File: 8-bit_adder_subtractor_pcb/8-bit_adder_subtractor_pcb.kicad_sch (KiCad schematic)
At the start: 6 parts, among them U1 74LS86, U2 74LS86, U3 74LS08, U4 74LS08, U5 74LS32, U6 74LS86

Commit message: Redesigned DDPT switch footprint
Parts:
- added D1, D2, D3, D4, D5, D6, D7, D8: ValueA, LED_THT:LED_D3.0mm, symbol Device:LED
- added D10, D11, D12, D13, D14, D15, D16, D9: ValueB, LED_THT:LED_D3.0mm, symbol Device:LED
- added D17, D18, D19, D20, D21, D22, D23, D24: Total, LED_THT:LED_D3.0mm, symbol Device:LED
- added D25: Subtraction, LED_THT:LED_D3.0mm, symbol Device:LED
- added D26: Addition, LED_THT:LED_D3.0mm, symbol Device:LED
- added R1, R10, R11, R12, R13, R14, R15, R16, R17, R18, R19, R2, R20, R21, R22, R23, R24, R25, R27, R3, R4, R5, R6, R7, R8, R9: 220, Resistor_THT:R_Axial_DIN0207_L6.3mm_D2.5mm_P7.62mm_Horizontal, symbol Device:R
- added R26: 10K, Resistor_THT:R_Axial_DIN0207_L6.3mm_D2.5mm_P7.62mm_Horizontal, symbol Device:R
- added SW1, SW10, SW11, SW12, SW13, SW14, SW15, SW16, SW17, SW2, SW3, SW4, SW5, SW6, SW7, SW8, SW9: SW_DPDT_x2, ddpt:SWITCH_S20203, symbol Switch:SW_DPDT_x2
- added U10, U7, U8: 74LS86, Package_DIP:DIP-14_W7.62mm, symbol 74xx:74LS86
- added U11, U9: 74LS08, Package_DIP:DIP-14_W7.62mm, symbol 74xx:74LS08
- added U12: 74LS32, Package_DIP:DIP-14_W7.62mm, symbol 74xx:74LS32
- U1, U2, U3, U4, U5, U6: footprint (none) -> Package_DIP:DIP-14_W7.62mm
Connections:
- net Cout0 is gone; now on net Cin1: U5.3
- net Cout1 is gone; now on net Cin2: U5.6
- net Cout2 is gone; now on net Cin3: U5.8
- net SL is gone; now on net Cin0: U6.1, U6.12, U6.4, U6.9
- net A0: now also R1.1, SW1.3 (C), SW1.6 (C)
- net A1: now also R2.1, SW2.3 (C), SW2.6 (C)
- net A2: now also R3.1, SW3.3 (C), SW3.6 (C)
- net A3: now also R4.1, SW4.3 (C), SW4.6 (C)
- net B0: now also R9.1, SW9.3 (C), SW9.6 (C)
- net B1: now also R10.1, SW10.3 (C), SW10.6 (C)
- net B2: now also R11.1, SW11.3 (C), SW11.6 (C)
- net B3: now also R12.1, SW12.3 (C), SW12.6 (C)
- net Cin0: now also R25.1, R26.1, SW17.3 (C), SW17.6 (C), U7.1, U7.12, U7.4, U7.9
- net VCC: now reaches U5.14 (VCC)
- net VCC: now also U1.14 (VCC), U2.14 (VCC), U3.14 (VCC), U4.14 (VCC), U6.14 (VCC), SW1.2 (B), SW1.5 (B), SW10.2 (B), SW10.5 (B), SW11.2 (B), SW11.5 (B), SW12.2 (B), SW12.5 (B), SW13.2 (B), SW13.5 (B), SW14.2 (B), SW14.5 (B), SW15.2 (B), SW15.5 (B), SW16.2 (B), SW16.5 (B), SW17.2 (B), SW17.5 (B), SW2.2 (B), SW2.5 (B), SW3.2 (B), SW3.5 (B), SW4.2 (B), SW4.5 (B), SW5.2 (B), SW5.5 (B), SW6.2 (B), SW6.5 (B), SW7.2 (B), SW7.5 (B), SW8.2 (B), SW8.5 (B), SW9.2 (B), SW9.5 (B), U10.14 (VCC), U11.14 (VCC), U12.14 (VCC), U7.14 (VCC), U8.14 (VCC), U9.14 (VCC)
- net GND: now reaches U5.7 (GND)
- net GND: now also U1.7 (GND), U2.7 (GND), U3.7 (GND), U4.7 (GND), U6.7 (GND), D1.1 (K), D10.1 (K), D11.1 (K), D12.1 (K), D13.1 (K), D14.1 (K), D15.1 (K), D16.1 (K), D17.1 (K), D18.1 (K), D19.1 (K), D2.1 (K), D20.1 (K), D21.1 (K), D22.1 (K), D23.1 (K), D24.1 (K), D25.1 (K), D26.1 (K), D3.1 (K), D4.1 (K), D5.1 (K), D6.1 (K), D7.1 (K), D8.1 (K), D9.1 (K), R26.2, U10.7 (GND), U11.7 (GND), U12.7 (GND), U7.7 (GND), U8.7 (GND), U9.7 (GND)
- net S3: now reaches U2.11
- net S3: now also R20.1
- net S0: now reaches U2.3
- net S0: now also R17.1
- net S2: now reaches U2.8
- net S2: now also R19.1
- net S1: now reaches U2.6
- net S1: now also R18.1
- net Cout3 renamed Cin4
- net Cin4: now also U10.2, U11.1
- new net: D17.2 (A), R17.2
- new net: SW3.1 (A), SW3.4 (A)
- new net: SW11.1 (A), SW11.4 (A)
- new net: SW4.1 (A), SW4.4 (A)
- new net: SW13.1 (A), SW13.4 (A)
- new net: SW15.1 (A), SW15.4 (A)
- new net: D2.2 (A), R2.2
- new net: D15.2 (A), R15.2
- new net: SW6.1 (A), SW6.4 (A)
- new net: D11.2 (A), R11.2
- new net: SW2.1 (A), SW2.4 (A)
- new net: U10.1, U11.2, U8.3
- new net: U11.3, U12.2
- new net: D22.2 (A), R22.2
- new net: D24.2 (A), R24.2
- new net: SW10.1 (A), SW10.4 (A)
- new net: U10.12, U11.13, U8.11
- new net: U7.11, U8.13, U9.13
- new net: D21.2 (A), R21.2
- new net: D14.2 (A), R14.2
- new net: U11.11, U12.13
- new net: D8.2 (A), R8.2
- new net: D1.2 (A), R1.2
- new net: U7.8, U8.10, U9.10
- new net: U10.9, U11.10, U8.8
- new net: SW7.1 (A), SW7.4 (A)
- new net: U12.4, U9.6
- new net: U11.6, U12.5
- new net: SW5.1 (A), SW5.4 (A)
- new net: D19.2 (A), R19.2
- new net: D16.2 (A), R16.2
- new net: D12.2 (A), R12.2
- new net: D7.2 (A), R7.2
- new net: U7.6, U8.5, U9.5
- new net: SW9.1 (A), SW9.4 (A)
- new net: U7.3, U8.2, U9.2
- new net: U12.1, U9.3
- new net: R27.1, SW17.1 (A), SW17.4 (A)
- new net: U12.9, U9.8
- new net: D26.2 (A), R27.2
- new net: U10.4, U11.5, U8.6
- new net: D9.2 (A), R9.2
- new net: D25.2 (A), R25.2
- new net: D6.2 (A), R6.2
- new net: SW16.1 (A), SW16.4 (A)
- new net: SW1.1 (A), SW1.4 (A)
- new net: D18.2 (A), R18.2
- new net: D3.2 (A), R3.2
- new net: D20.2 (A), R20.2
- new net: D23.2 (A), R23.2
- new net: SW8.1 (A), SW8.4 (A)
- new net: D10.2 (A), R10.2
- new net: D5.2 (A), R5.2
- new net: D4.2 (A), R4.2
- new net: U11.8, U12.10
- new net: D13.2 (A), R13.2
- new net: SW14.1 (A), SW14.4 (A)
- new net: U12.12, U9.11
- new net: SW12.1 (A), SW12.4 (A)
- new net A4: R5.1, SW5.3 (C), SW5.6 (C), U8.1, U9.1
- new net A5: R6.1, SW6.3 (C), SW6.6 (C), U8.4, U9.4
- new net A6: R7.1, SW7.3 (C), SW7.6 (C), U8.9, U9.9
- new net A7: R8.1, SW8.3 (C), SW8.6 (C), U8.12, U9.12
- new net B4: R13.1, SW13.3 (C), SW13.6 (C), U7.2
- new net B5: R14.1, SW14.3 (C), SW14.6 (C), U7.5
- new net B6: R15.1, SW15.3 (C), SW15.6 (C), U7.10
- new net B7: R16.1, SW16.3 (C), SW16.6 (C), U7.13
- new net Cin5: U10.5, U11.4, U12.3
- new net Cin6: U10.10, U11.9, U12.6
- new net Cin7: U10.13, U11.12, U12.8
- new net Cout7: U12.11
- new net S4: R21.1, U10.3
- new net S5: R22.1, U10.6
- new net S6: R23.1, U10.8
- new net S7: R24.1, U10.11
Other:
- note added: "When the switch is turned on then the select and Cin0 is tied to Vcc and the circuit acts as subtractor."
- moved on the sheet: U1E, U2A, U2B, U2C, U2D, U2E, U3E, U4A, U4B, U4C, U4D, U4E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

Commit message: added the pcb files
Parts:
- added D27: Carry, LED_THT:LED_D3.0mm, symbol Device:LED
- added J1: Barrel_Jack, Connector_BarrelJack:BarrelJack_Horizontal, symbol Connector:Barrel_Jack
- added R28: 220, Resistor_THT:R_Axial_DIN0207_L6.3mm_D2.5mm_P7.62mm_Horizontal, symbol Device:R
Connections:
- net A0: now also SW1.2 (B), SW1.5 (B); no longer SW1.3 (C), SW1.6 (C)
- net A1: now also SW2.2 (B), SW2.5 (B); no longer SW2.3 (C), SW2.6 (C)
- net A2: now also SW3.2 (B), SW3.5 (B); no longer SW3.3 (C), SW3.6 (C)
- net A3: now also SW4.2 (B), SW4.5 (B); no longer SW4.3 (C), SW4.6 (C)
- net A4: now also SW5.2 (B), SW5.5 (B); no longer SW5.3 (C), SW5.6 (C)
- net A5: now also SW6.2 (B), SW6.5 (B); no longer SW6.3 (C), SW6.6 (C)
- net A6: now also SW7.2 (B), SW7.5 (B); no longer SW7.3 (C), SW7.6 (C)
- net A7: now also SW8.2 (B), SW8.5 (B); no longer SW8.3 (C), SW8.6 (C)
- net B0: now also SW9.2 (B), SW9.5 (B); no longer SW9.3 (C), SW9.6 (C)
- net B1: now also SW10.2 (B), SW10.5 (B); no longer SW10.3 (C), SW10.6 (C)
- net B2: now also SW11.2 (B), SW11.5 (B); no longer SW11.3 (C), SW11.6 (C)
- net B3: now also SW12.2 (B), SW12.5 (B); no longer SW12.3 (C), SW12.6 (C)
- net B4: now also SW13.2 (B), SW13.5 (B); no longer SW13.3 (C), SW13.6 (C)
- net B5: now also SW14.2 (B), SW14.5 (B); no longer SW14.3 (C), SW14.6 (C)
- net B6: now also SW15.2 (B), SW15.5 (B); no longer SW15.3 (C), SW15.6 (C)
- net B7: now also SW16.2 (B), SW16.5 (B); no longer SW16.3 (C), SW16.6 (C)
- net Cout7: now also R28.1
- net GND: now also SW1.1 (A), SW1.4 (A), SW10.1 (A), SW10.4 (A), SW11.1 (A), SW11.4 (A), SW12.1 (A), SW12.4 (A), SW13.1 (A), SW13.4 (A), SW14.1 (A), SW14.4 (A), SW15.1 (A), SW15.4 (A), SW16.1 (A), SW16.4 (A), SW2.1 (A), SW2.4 (A), SW3.1 (A), SW3.4 (A), SW4.1 (A), SW4.4 (A), SW5.1 (A), SW5.4 (A), SW6.1 (A), SW6.4 (A), SW7.1 (A), SW7.4 (A), SW8.1 (A), SW8.4 (A), SW9.1 (A), SW9.4 (A), D27.1 (K), J1.2
- net VCC: now also SW1.3 (C), SW1.6 (C), SW10.3 (C), SW10.6 (C), SW11.3 (C), SW11.6 (C), SW12.3 (C), SW12.6 (C), SW13.3 (C), SW13.6 (C), SW14.3 (C), SW14.6 (C), SW15.3 (C), SW15.6 (C), SW16.3 (C), SW16.6 (C), SW2.3 (C), SW2.6 (C), SW3.3 (C), SW3.6 (C), SW4.3 (C), SW4.6 (C), SW5.3 (C), SW5.6 (C), SW6.3 (C), SW6.6 (C), SW7.3 (C), SW7.6 (C), SW8.3 (C), SW8.6 (C), SW9.3 (C), SW9.6 (C), J1.1; no longer SW1.2 (B), SW1.5 (B), SW10.2 (B), SW10.5 (B), SW11.2 (B), SW11.5 (B), SW12.2 (B), SW12.5 (B), SW13.2 (B), SW13.5 (B), SW14.2 (B), SW14.5 (B), SW15.2 (B), SW15.5 (B), SW16.2 (B), SW16.5 (B), SW2.2 (B), SW2.5 (B), SW3.2 (B), SW3.5 (B), SW4.2 (B), SW4.5 (B), SW5.2 (B), SW5.5 (B), SW6.2 (B), SW6.5 (B), SW7.2 (B), SW7.5 (B), SW8.2 (B), SW8.5 (B), SW9.2 (B), SW9.5 (B)
- net Cin0 renamed SL
- new net: D27.2 (A), R28.2
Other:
- moved on the sheet: SW10A, SW10B, SW11A, SW11B, SW12A, SW12B, SW13A, SW13B, SW14A, SW14B, SW15A, SW15B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

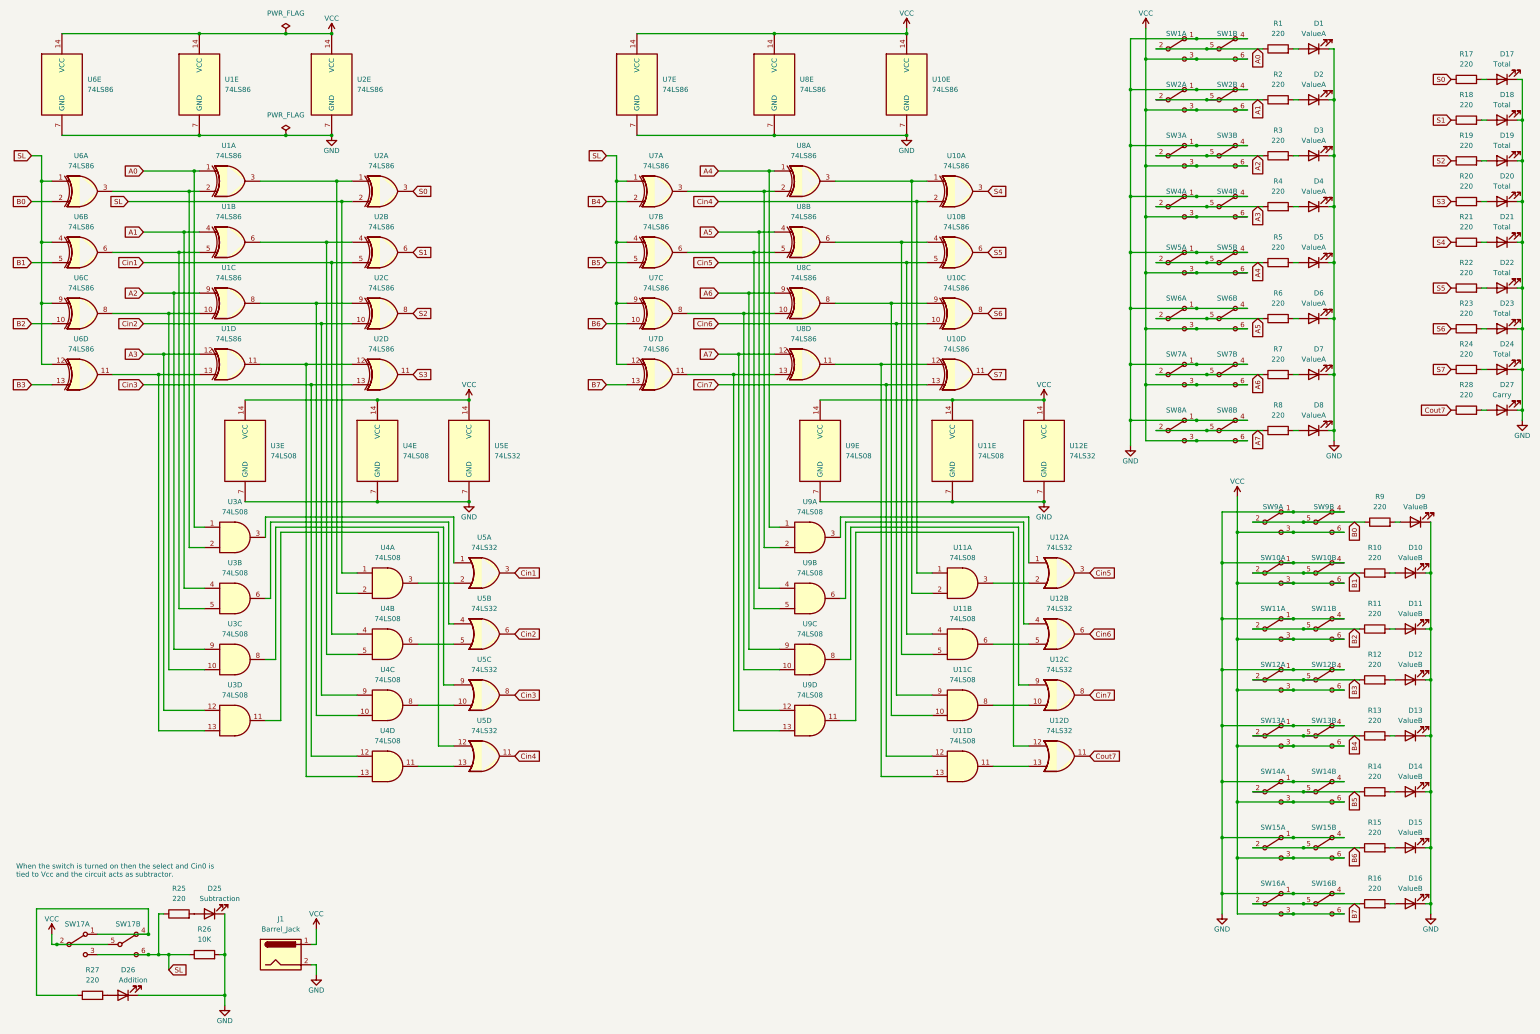
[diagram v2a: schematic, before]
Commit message: Edited the Silkscreen for LAB448
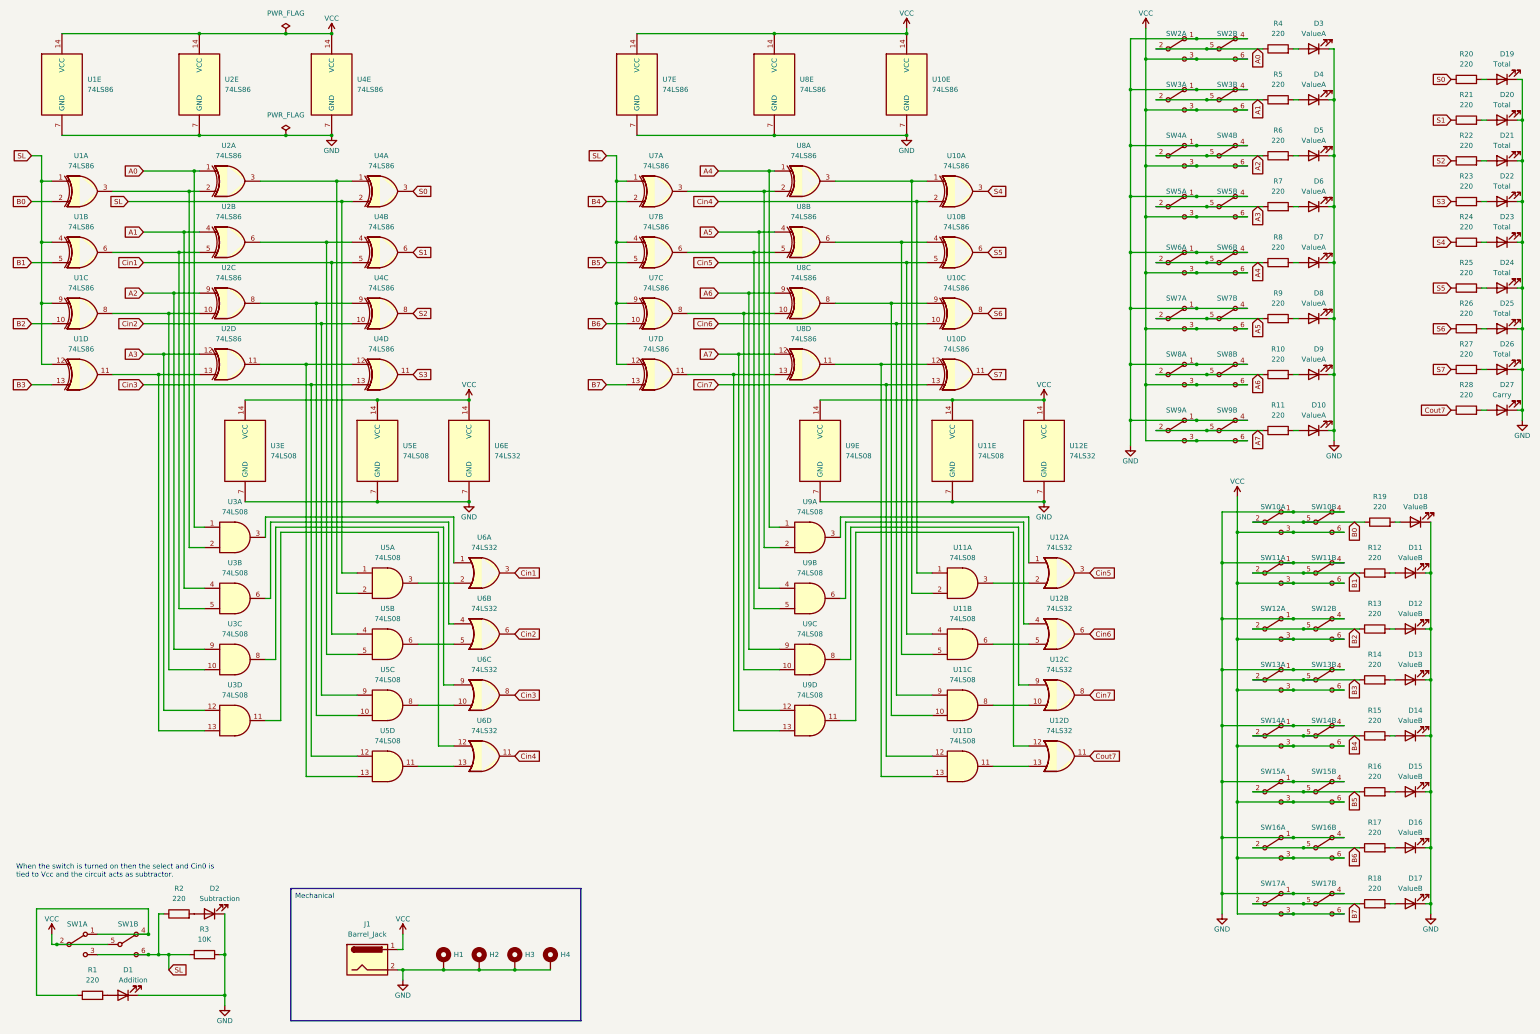
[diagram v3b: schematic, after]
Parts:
- added H1, H2, H3, H4: MountingHole_Pad, MountingHole:MountingHole_3mm_Pad, symbol Mechanical:MountingHole_Pad
- renumbered D26 to D1, D8 to D10, D10 to D11, D11 to D12, D12 to D13, D13 to D14, D14 to D15, D15 to D16, D16 to D17, D9 to D18, D17 to D19, D25 to D2, D18 to D20, D19 to D21, D20 to D22, D21 to D23, D22 to D24, D23 to D25, D24 to D26, D1 to D3, D2 to D4, D3 to D5, D4 to D6, D5 to D7, D6 to D8, D7 to D9, R27 to R1, R7 to R10, R8 to R11, R10 to R12, R11 to R13, R12 to R14, R13 to R15, R14 to R16, R15 to R17, R16 to R18, R9 to R19, R25 to R2, R17 to R20, R18 to R21, R19 to R22, R20 to R23, R21 to R24, R22 to R25, R23 to R26, R24 to R27, R26 to R3, R1 to R4, R2 to R5, R3 to R6, R4 to R7, R5 to R8, R6 to R9, SW17 to SW1, SW9 to SW10, SW10 to SW11, SW11 to SW12, SW12 to SW13, SW13 to SW14, SW14 to SW15, SW15 to SW16, SW16 to SW17, SW1 to SW2, SW2 to SW3, SW3 to SW4, SW4 to SW5, SW5 to SW6, SW6 to SW7, SW7 to SW8, SW8 to SW9, U6 to U1, U1 to U2, U2 to U4, U4 to U5, U5 to U6
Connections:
- net GND: now also H1.1, H2.1, H3.1, H4.1
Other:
- moved on the sheet: J1
